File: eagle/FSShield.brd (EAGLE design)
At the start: 111.4 x 58.4 mm, 37 parts, among them J1 057-040-1, J2 057-040-1, U1 LM7322QMAX/NOPB, X1 C-GRID-03-70543

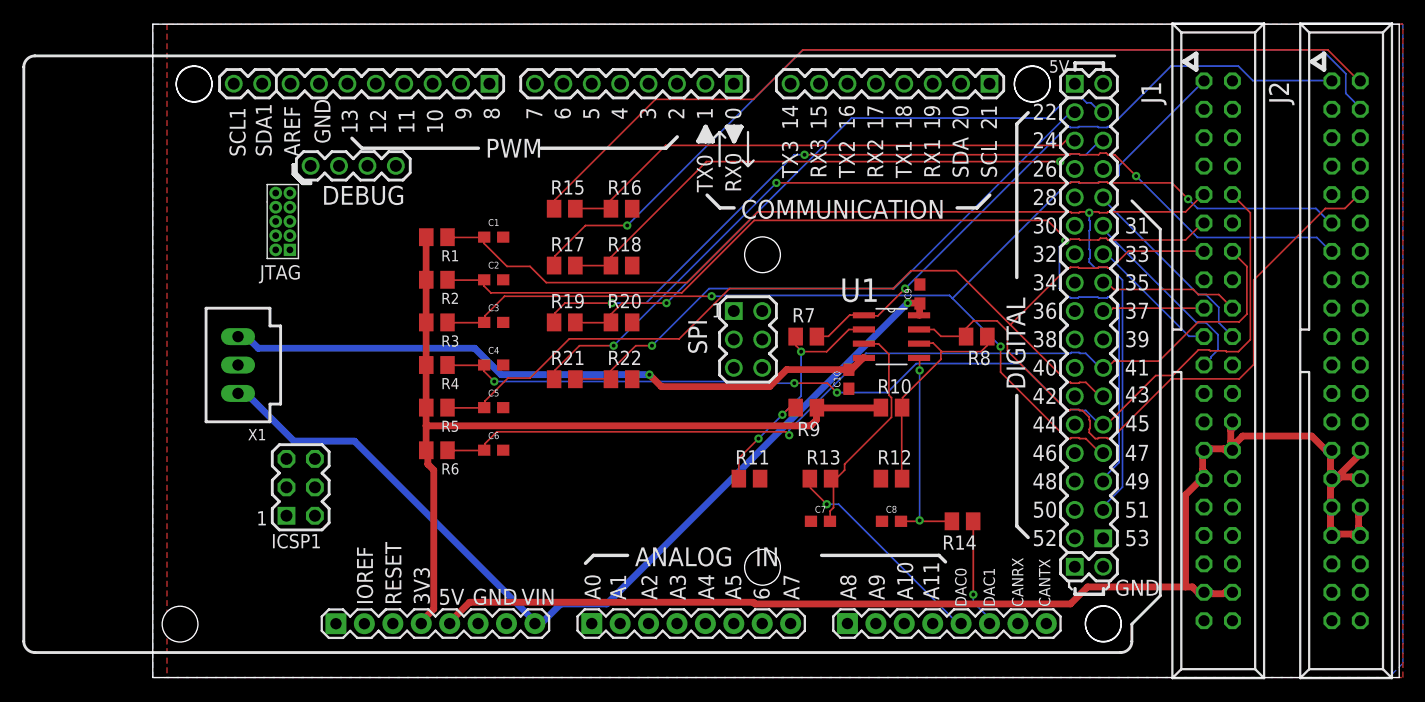
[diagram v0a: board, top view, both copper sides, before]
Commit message: removed DAC code. Updated eagle files.
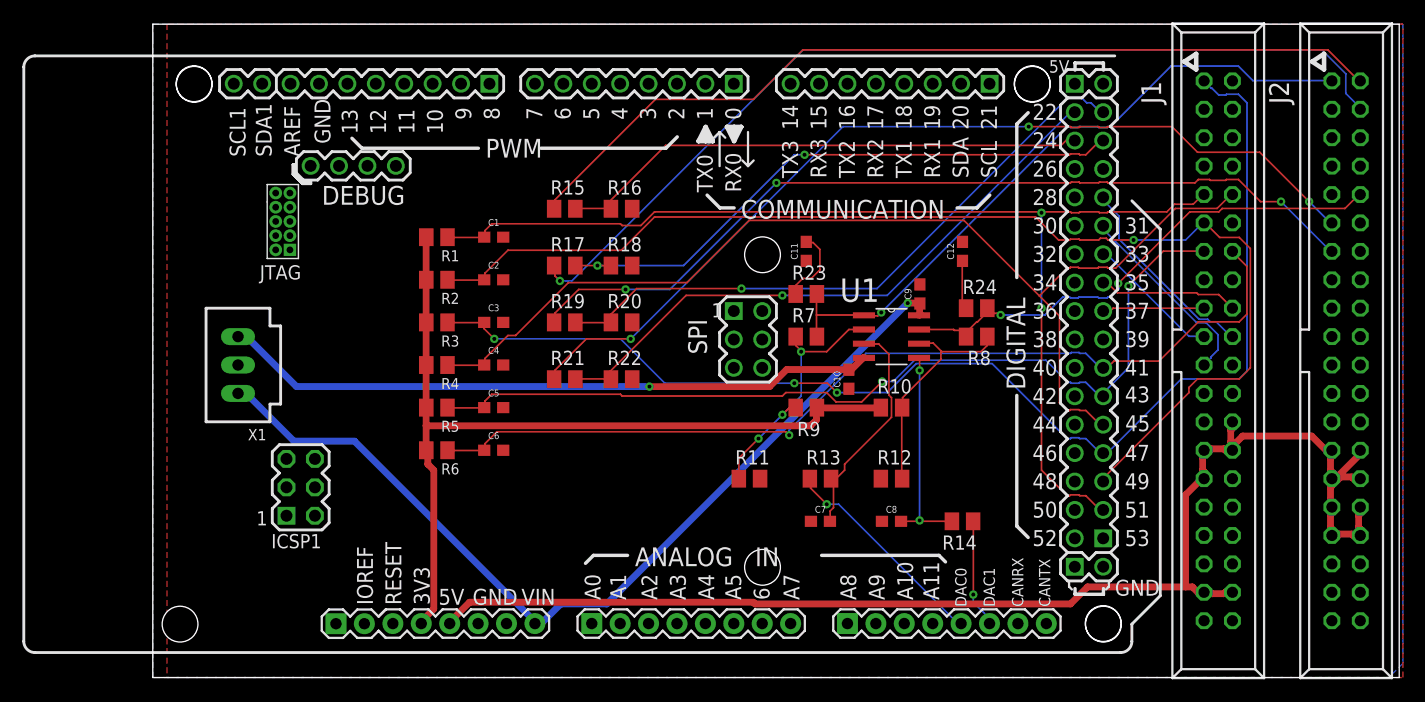
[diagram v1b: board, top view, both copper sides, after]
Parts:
- added C11, C12: 0.1uF, SparkFun-Capacitors:0603
- added R23, R24: 10, resistor:M0805
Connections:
- new net N$5: C12.1, R24.1
- new net N$6: C11.2, R23.1
- net GND: now also C11.1, C12.2
- net SIG0: now also R23.2
- net SIG1: now also R24.2
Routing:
- net SIG1: track 60.6 -> 47.2 mm, vias 0 -> 2
- net DI_STOP: track 98.3 -> 110.6 mm, vias 2 -> 3
- net DI_CANOPY: track 88.9 -> 81.8 mm, vias 0 -> 2
- net N$6: track 0.00 -> 6.87 mm
- net DI_HOME: track 99.8 -> 105.5 mm
- net N$5: track 0.00 -> 4.40 mm
- net B1: track 78.9 -> 83.0 mm
- net DI_BOTTOM: track 93.5 -> 97.6 mm, vias 3 -> 0
- net SIG0: track 56.8 -> 59.9 mm
- net DI_TOP_A: track 102.7 -> 100.0 mm, vias 1 -> 2
- net A1: track 80.0 -> 78.2 mm
- net B0: track 83.8 -> 85.0 mm
- net P_B: track 52.3 -> 53.1 mm, vias 1 -> 2
